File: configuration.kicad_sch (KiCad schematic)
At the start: 1 part, among them SW1 SW_DIP_x04

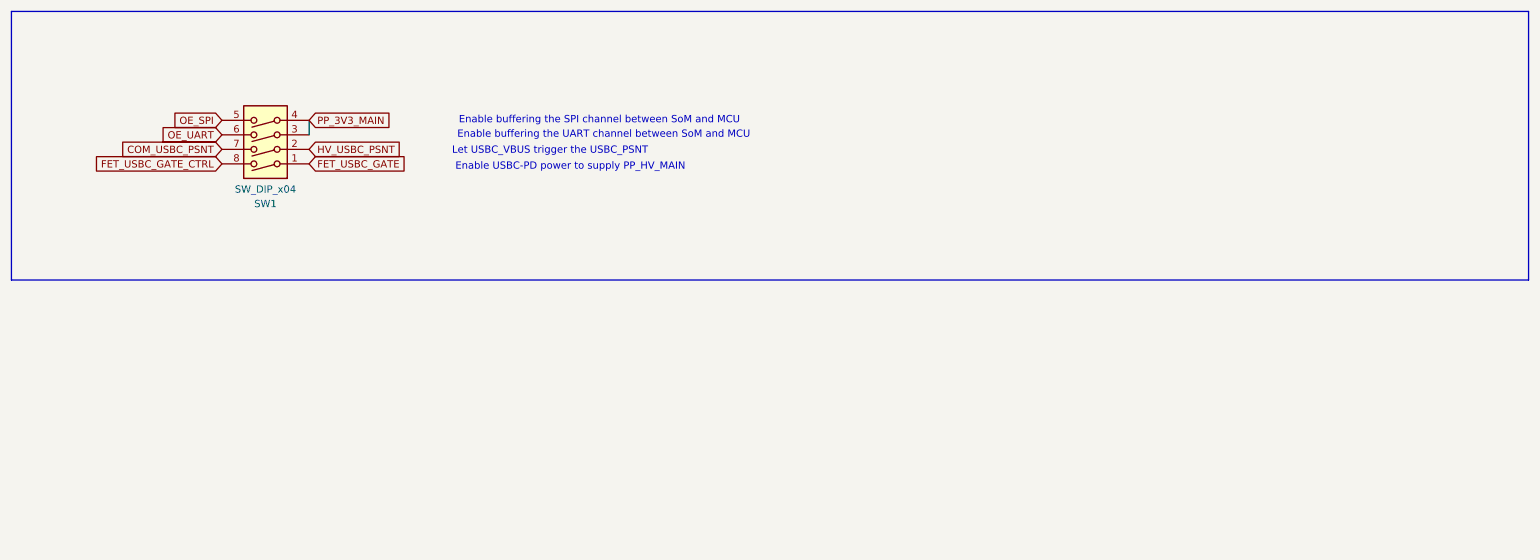
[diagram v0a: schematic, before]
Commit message: Complete schematic transfer
Signed-off-by: Matthew Guo <matthew@botbuilt.com>
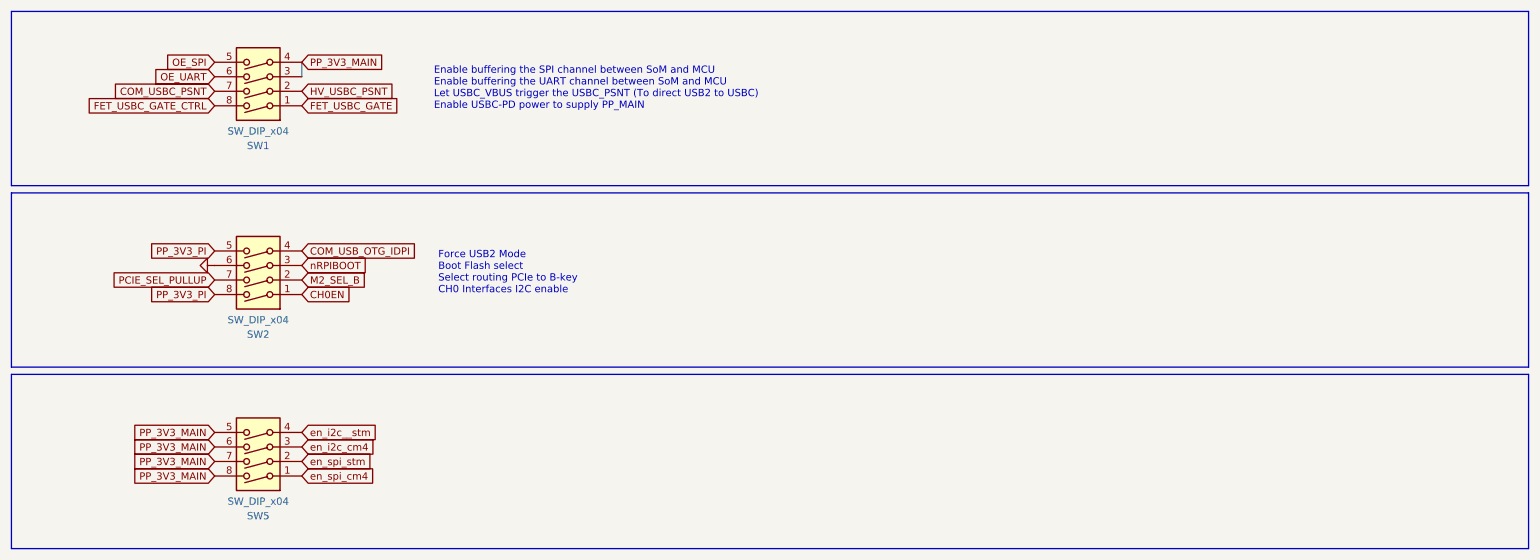
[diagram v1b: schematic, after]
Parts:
- added SW2, SW5: SW_DIP_x04, Button_Switch_SMD:SW_DIP_SPSTx04_Slide_Copal_CHS-04A_W5.08mm_P1.27mm_JPin, symbol Switch:SW_DIP_x04
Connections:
- net PP_3V3_MAIN: now also SW5.5, SW5.6, SW5.7, SW5.8
- new net CH0EN: SW2.1
- new net COM_USB_OTG_IDPI: SW2.4
- new net GND: SW2.6
- new net M2_SEL_B: SW2.2
- new net PCIE_SEL_PULLUP: SW2.7
- new net PP_3V3_PI: SW2.5, SW2.8
- new net en_i2c__stm: SW5.4
- new net en_i2c_cm4: SW5.3
- new net en_spi_cm4: SW5.1
- new net en_spi_stm: SW5.2
- new net nRPIBOOT: SW2.3
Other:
- note added: "Enable buffering the SPI channel between SoM and MCU Enable buffering the UART channel between SoM and MCU Let USBC_VBUS trigger the USBC_PSNT (To direct USB2 to USBC) Enable USBC-PD power to supply PP_MAIN"
- note added: "Force USB2 Mode Boot Flash select Select routing PCIe to B-key CH0 Interfaces I2C enable"
- note removed: "Enable USBC-PD power to supply PP_HV_MAIN"
- note removed: "Enable buffering the SPI channel between SoM and MCU"
- note removed: "Enable buffering the UART channel between SoM and MCU"
- note removed: "Let USBC_VBUS trigger the USBC_PSNT"
- moved on the sheet: SW1
